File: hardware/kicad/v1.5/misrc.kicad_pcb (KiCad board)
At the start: 2 copper layers, 146.2 x 72.6 mm, 194 parts, among them J1 Conn_01x01_Shielded, J2 Conn_01x08_Socket, J201 DOSIN-801-0050, J3 GPIFII_J6, J4 GPIFII_J7, Q1 FZT690B, Q101 CMPT5179, Q102 CMPT5179, Q2 FZT790A, Q201 CMPT5179, Q202 CMPT5179, SW1 SW_Push, SW101 SW_DIP_x04, SW102 SW_DIP_x03, SW103 SW_DIP_x03, SW104 SW_DIP_x03, SW105 SW_DIP_x02, SW2 SW_DIP_x01, SW201 SW_DIP_x04, SW202 SW_DIP_x03, SW203 SW_DIP_x03, SW204 SW_DIP_x03, SW205 SW_DIP_x02, U1 4043, U101 AD8138ARZ, U102 AD9235, U2 74VHC541, U201 AD8138ARZ, U202 AD9235, U3 74VHC541, U4 74VHC541, U5 74VHC541, U6 TPS60401, U7 ADP7156ARDZ, X1 40M

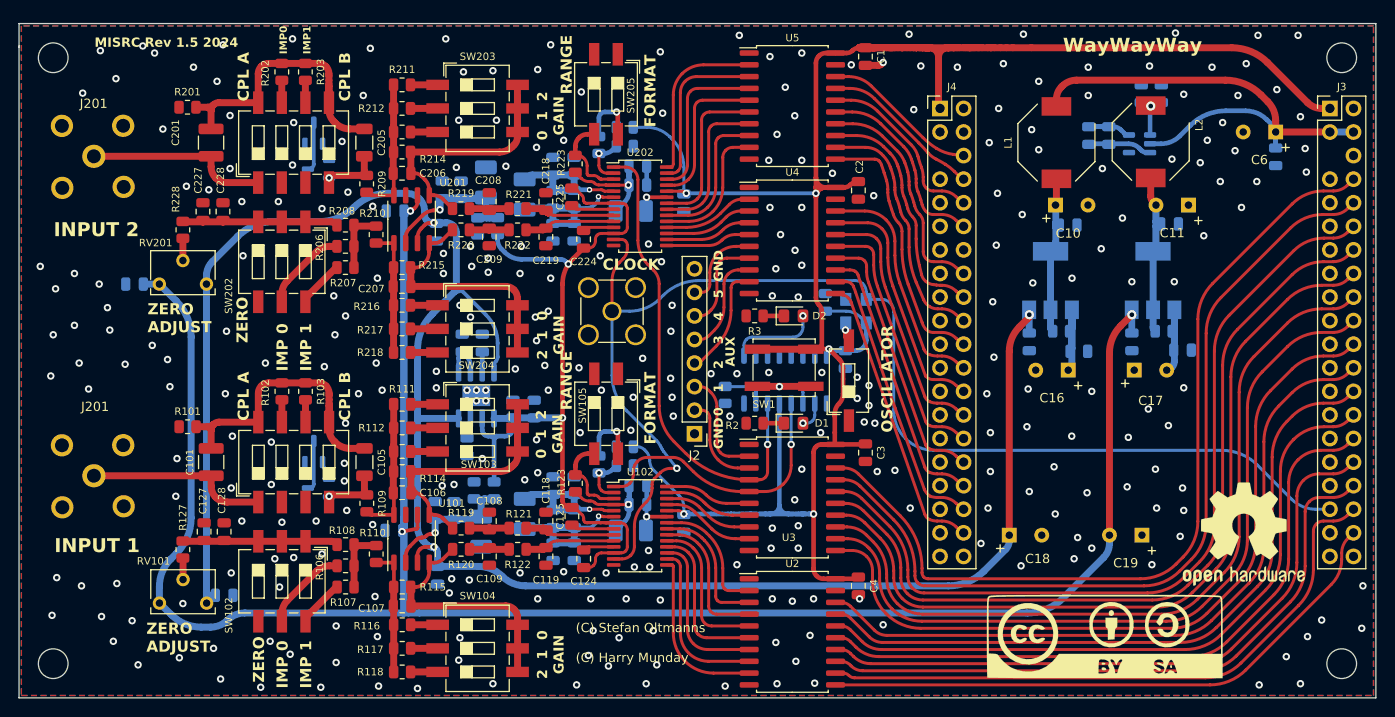
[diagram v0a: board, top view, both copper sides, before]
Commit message: V1.5a production changes, change crystal to one with higher load abbilitys
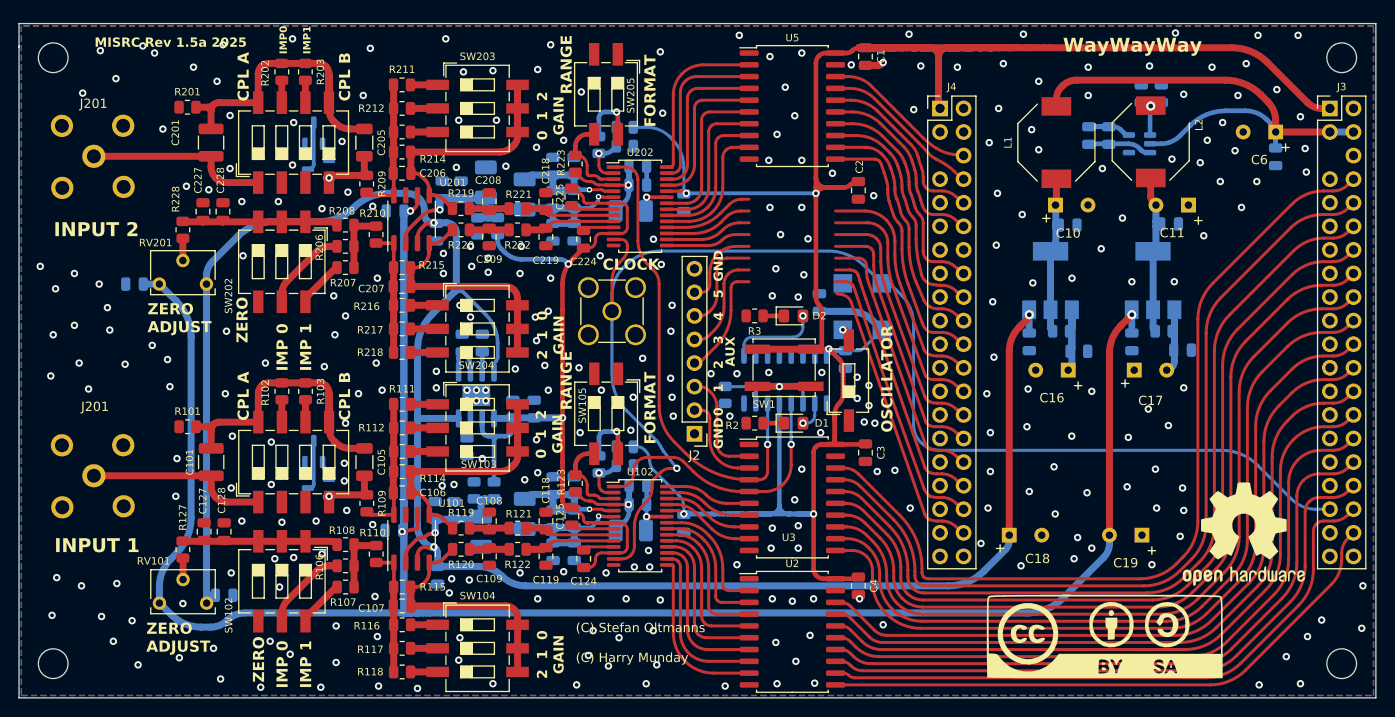
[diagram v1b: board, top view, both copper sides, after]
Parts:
- removed U4: 74VHC541, Package_SO:SOIC-20W_7.5x12.8mm_P1.27mm
- X1: footprint Oscillator:Oscillator_SMD_EuroQuartz_XO53-4Pin_5.0x3.2mm -> Oscillator:Oscillator_SMD_EuroQuartz_XO91-4Pin_7.0x5.0mm
- moved X1 0.84 mm to (151.4, 93.7)
- moved C31 0.64 mm to (146.8, 93.3)
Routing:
- net /Input_ADC_CH1/CLK: track 138.2 -> 143.8 mm
- net VDD: track 229.7 -> 232.7 mm
- net -5VA: track 223.0 -> 224.6 mm
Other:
- board text added: "MISRC Rev 1.5a 2025"
- board text removed: "MISRC Rev 1.5 2024"

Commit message: Fix V1.5a gerbers
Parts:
- added ?: , , F.Cu at (201.8, 77.5)
- added ?: , , F.Cu at (159.8, 77.5)
- added U4: 74VHC541, Package_SO:SOIC-20W_7.5x12.8mm_P1.27mm, F.Cu at (143.9, 86.6)
- renumbered J201 to J202
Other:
- board text added: "AUX Inputs"
- board text added: "CLOCK OUT"
- board text removed: "AUX"
- board text removed: "CLOCK"
